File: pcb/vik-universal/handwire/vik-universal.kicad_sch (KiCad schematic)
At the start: 5 parts, among them J1001 Conn_01x01_Socket, J1002 Conn_01x01_Socket

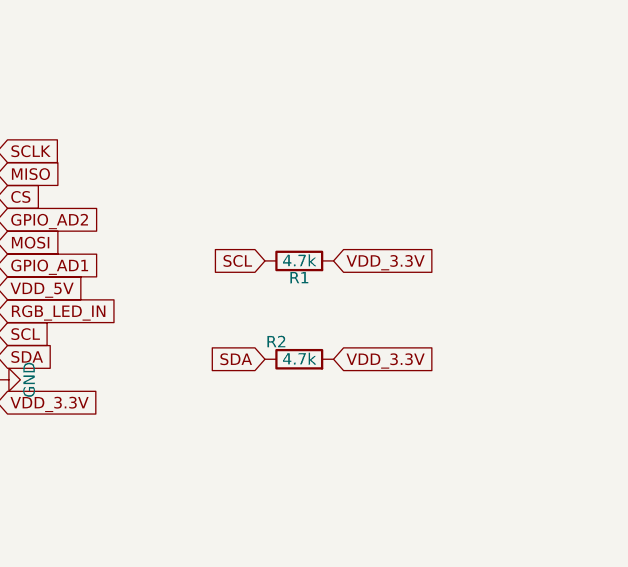
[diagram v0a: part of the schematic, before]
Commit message: vik universal handwire - added jumpers to enable or disable I2C pull up resistors
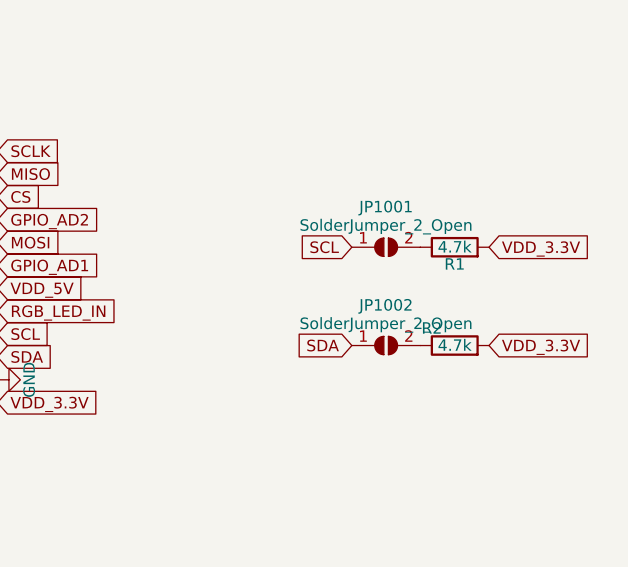
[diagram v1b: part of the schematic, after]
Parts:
- added JP1001, JP1002: SolderJumper_2_Open, Jumper:SolderJumper-2_P1.3mm_Open_RoundedPad1.0x1.5mm, symbol Jumper:SolderJumper_2_Open
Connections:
- net SCL: now also JP1001.1 (A); no longer R1.1
- net SDA: now also JP1002.1 (A); no longer R2.1
- new net: JP1001.2 (B), R1.1
- new net: JP1002.2 (B), R2.1
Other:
- moved on the sheet: R1, R2
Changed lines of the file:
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@@
     )
   )
-  (global_label "SCL" (shape input) (at 222.758 71.374 180)
-    (effects (font (size 1.27 1.27)) (justify right))
-    (property "Intersheetrefs" "${INTERSHEET_REFS}" (at 216.5349 71.4534 0)
+  (global_label "SCL" (shape input) (at 232.41 69.85 180)
+    (effects (font (size 1.27 1.27)) (justify right))
+    (property "Intersheetrefs" "${INTERSHEET_REFS}" (at 226.1869 69.9294 0)
       (effects (font (size 1.27 1.27)) (justify right) hide)
     )
@@
     )
   )
-  (global_label "VDD_3.3V" (shape input) (at 230.378 71.374 0)
-    (effects (font (size 1.27 1.27)) (justify left))
-    (property "Intersheetrefs" "${INTERSHEET_REFS}" (at 241.4997 71.2946 0)
+  (global_label "VDD_3.3V" (shape input) (at 247.65 69.85 0)
+    (effects (font (size 1.27 1.27)) (justify left))
+    (property "Intersheetrefs" "${INTERSHEET_REFS}" (at 258.7717 69.7706 0)
       (effects (font (size 1.27 1.27)) (justify left) hide)
     )
@@
     )
   )
-  (global_label "VDD_3.3V" (shape input) (at 230.378 82.296 0)
-    (effects (font (size 1.27 1.27)) (justify left))
-    (property "Intersheetrefs" "${INTERSHEET_REFS}" (at 241.4997 82.2166 0)
-      (effects (font (size 1.27 1.27)) (justify left) hide)
-    )
-  )
-  (global_label "SDA" (shape input) (at 222.758 82.296 180)
-    (effects (font (size 1.27 1.27)) (justify right))
-    (property "Intersheetrefs" "${INTERSHEET_REFS}" (at 216.5349 82.3754 0)
+  (global_label "VDD_3.3V" (shape input) (at 247.65 80.772 0)
+    (effects (font (size 1.27 1.27)) (justify left))
+    (property "Intersheetrefs" "${INTERSHEET_REFS}" (at 258.7717 80.6926 0)
+      (effects (font (size 1.27 1.27)) (justify left) hide)
+    )
+  )
+  (global_label "SDA" (shape input) (at 232.41 80.772 180)
+    (effects (font (size 1.27 1.27)) (justify right))
+    (property "Intersheetrefs" "${INTERSHEET_REFS}" (at 226.1869 80.8514 0)
       (effects (font (size 1.27 1.27)) (justify right) hide)
     )
@@
     )
   )
-  (symbol (lib_id "Device:R") (at 226.568 71.374 90) (unit 1)
+  (symbol (lib_id "Device:R") (at 243.84 69.85 90) (unit 1)
     (in_bom yes) (on_board yes) (dnp no)
-    (property "Reference" "R1" (at 226.568 73.279 90)
-      (effects (font (size 1.27 1.27)))
-    )
-    (property "Value" "4.7k" (at 226.568 71.374 90)
-      (effects (font (size 1.27 1.27)))
-    )
-    (property "Footprint" "fingerpunch:D3_TH_SMD" (at 226.568 73.152 90)
-      (effects (font (size 1.27 1.27)) hide)
-    )
-    (property "Datasheet" "~" (at 226.568 71.374 0)
-      (effects (font (size 1.27 1.27)) hide)
-    )
-    (property "LCSC" "C104821" (at 226.568 71.374 90)
+    (property "Reference" "R1" (at 243.84 71.755 90)
+      (effects (font (size 1.27 1.27)))
+    )
+    (property "Value" "4.7k" (at 243.84 69.85 90)
+      (effects (font (size 1.27 1.27)))
+    )
+    (property "Footprint" "fingerpunch:D3_TH_SMD" (at 243.84 71.628 90)
+      (effects (font (size 1.27 1.27)) hide)
+    )
+    (property "Datasheet" "~" (at 243.84 69.85 0)
+      (effects (font (size 1.27 1.27)) hide)
+    )
+    (property "LCSC" "C104821" (at 243.84 69.85 90)
       (effects (font (size 1.27 1.27)) hide)
     )
@@
     )
   )
+  (symbol (lib_id "Jumper:SolderJumper_2_Open") (at 236.22 69.85 0) (unit 1)
+    (in_bom yes) (on_board yes) (dnp no) (fields_autoplaced)
+    (property "Reference" "JP1001" (at 236.22 65.381 0)
+      (effects (font (size 1.27 1.27)))
+    )
+    (property "Value" "SolderJumper_2_Open" (at 236.22 67.429 0)
+      (effects (font (size 1.27 1.27)))
+    )
+    (property "Footprint" "Jumper:SolderJumper-2_P1.3mm_Open_RoundedPad1.0x1.5mm" (at 236.22 69.85 0)
+      (effects (font (size 1.27 1.27)) hide)
+    )
+    (property "Datasheet" "~" (at 236.22 69.85 0)
+      (effects (font (size 1.27 1.27)) hide)
+    )
+    (pin "1")
+    (pin "2")
+    (instances
+      (project "vik-universal"
+        (path "/e63e39d7-6ac0-4ffd-8aa3-1841a4541b55"
+          (reference "JP1001") (unit 1)
+        )
+      )
+    )
+  )
   (symbol (lib_id "Connector:Conn_01x12_Socket") (at 188.214 107.442 180) (unit 1)
     (in_bom yes) (on_board yes) (dnp no) (fields_autoplaced)
@@
     )
   )
-  (symbol (lib_id "Device:R") (at 226.568 82.296 90) (unit 1)
+  (symbol (lib_id "Jumper:SolderJumper_2_Open") (at 236.22 80.772 0) (unit 1)
+    (in_bom yes) (on_board yes) (dnp no) (fields_autoplaced)
+    (property "Reference" "JP1002" (at 236.22 76.303 0)
+      (effects (font (size 1.27 1.27)))
+    )
+    (property "Value" "SolderJumper_2_Open" (at 236.22 78.351 0)
+      (effects (font (size 1.27 1.27)))
+    )
+    (property "Footprint" "Jumper:SolderJumper-2_P1.3mm_Open_RoundedPad1.0x1.5mm" (at 236.22 80.772 0)
+      (effects (font (size 1.27 1.27)) hide)
+    )
+    (property "Datasheet" "~" (at 236.22 80.772 0)
+      (effects (font (size 1.27 1.27)) hide)
+    )
+    (pin "1")
+    (pin "2")
+    (instances
+      (project "vik-universal"
+        (path "/e63e39d7-6ac0-4ffd-8aa3-1841a4541b55"
+          (reference "JP1002") (unit 1)
+        )
+      )
+    )
+  )
+  (symbol (lib_id "Device:R") (at 243.84 80.772 90) (unit 1)
     (in_bom yes) (on_board yes) (dnp no)
-    (property "Reference" "R2" (at 224.028 80.391 90)
-      (effects (font (size 1.27 1.27)))
-    )
-    (property "Value" "4.7k" (at 226.568 82.296 90)
-      (effects (font (size 1.27 1.27)))
-    )
-    (property "Footprint" "fingerpunch:D3_TH_SMD" (at 226.568 84.074 90)
-      (effects (font (size 1.27 1.27)) hide)
-    )
-    (property "Datasheet" "~" (at 226.568 82.296 0)
-      (effects (font (size 1.27 1.27)) hide)
-    )
-    (property "LCSC" "C104821" (at 226.568 82.296 90)
-      (effects (font (size 1.27 1.27)) hide)
-    )
+    (property "Reference" "R2" (at 241.3 78.867 90)
+      (effects (font (size 1.27 1.27)))
+    )
+    (property "Value" "4.7k" (at 243.84 80.772 90)
+      (effects (font (size 1.27 1.27)))
+    )
+    (property "Footprint" "fingerpunch:D3_TH_SMD" (at 243.84 82.55 90)
+      (effects (font (size 1.27 1.27)) hide)
+    )
+    (property "Datasheet" "~" (at 243.84 80.772 0)
+      (effects (font (size 1.27 1.27)) hide)
+    )
+    (property "LCSC" "C104821" (at 243.84 80.772 90)
+      (effects (font (size 1.27 1.27)) hide)
+    )

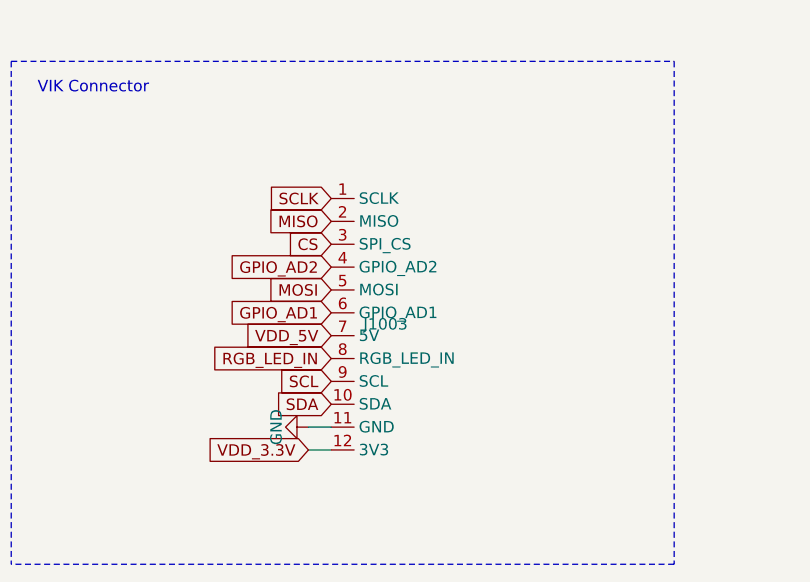
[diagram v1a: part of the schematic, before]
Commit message: updated vikm connector symbols, per some recommendations from sigprof in fingerpunch discord
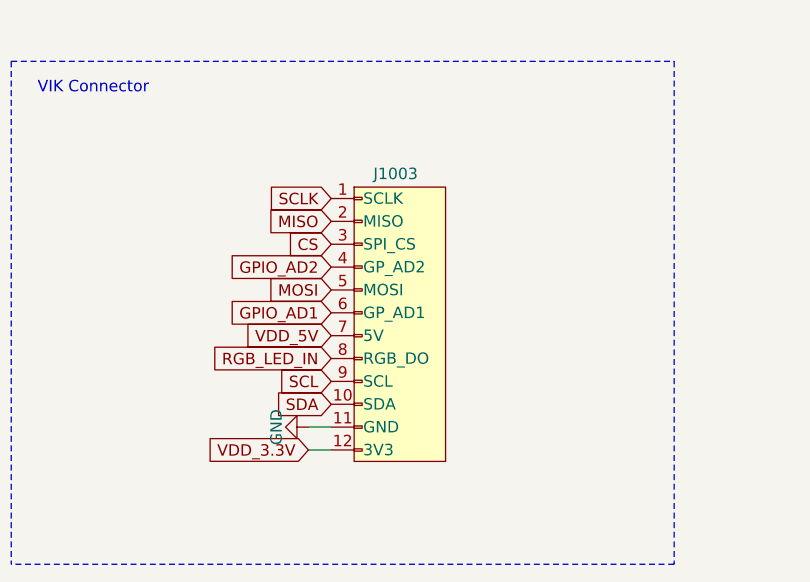
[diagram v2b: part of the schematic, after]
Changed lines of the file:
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@@
     )
   )
-  (symbol (lib_id "vik:vik-module-connector") (at 96.52 107.696 0) (unit 1)
-    (in_bom yes) (on_board yes) (dnp no) (fields_autoplaced)
-    (property "Reference" "J1003" (at 100.076 107.696 0)
+  (symbol (lib_id "vik:vik-module-connector") (at 104.14 106.426 0) (unit 1)
+    (in_bom yes) (on_board yes) (dnp no)
+    (property "Reference" "J1003" (at 101.1936 90.9828 0)
       (effects (font (size 1.27 1.27)) (justify left))
     )
-    (property "Value" "~" (at 96.52 101.346 0)
+    (property "Value" "~" (at 104.14 100.076 0)
       (effects (font (size 1.27 1.27)))
     )
-    (property "Footprint" "vik:vik-module-connector-horizontal" (at 96.52 101.346 0)
+    (property "Footprint" "vik:vik-module-connector-horizontal" (at 104.14 100.076 0)
       (effects (font (size 1.27 1.27)) hide)
     )
-    (property "Datasheet" "" (at 96.52 101.346 0)
+    (property "Datasheet" "" (at 104.14 100.076 0)
       (effects (font (size 1.27 1.27)) hide)
     )
-    (property "LCSC" "C2919557" (at 96.52 107.696 0)
+    (property "LCSC" "C2919557" (at 104.14 106.426 0)
       (effects (font (size 1.27 1.27)) hide)
     )
